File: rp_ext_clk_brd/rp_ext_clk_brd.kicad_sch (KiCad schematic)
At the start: 3 parts, among them J1 8526-4500PL, U1 SN65LVDS122D, Y1 AK7DAF1-125.0000

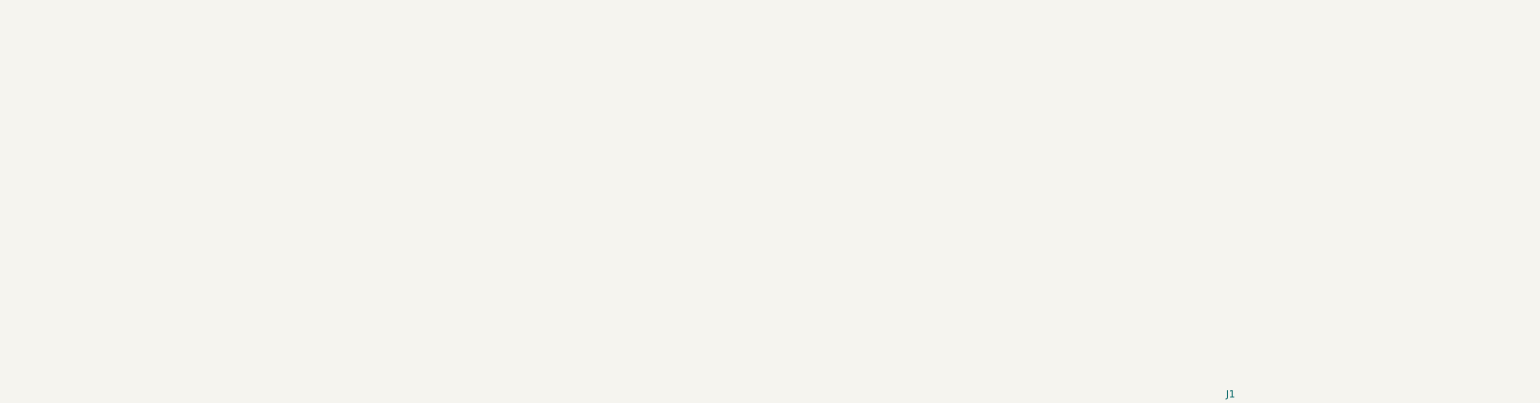
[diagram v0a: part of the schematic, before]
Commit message: adding decoupling and power supply
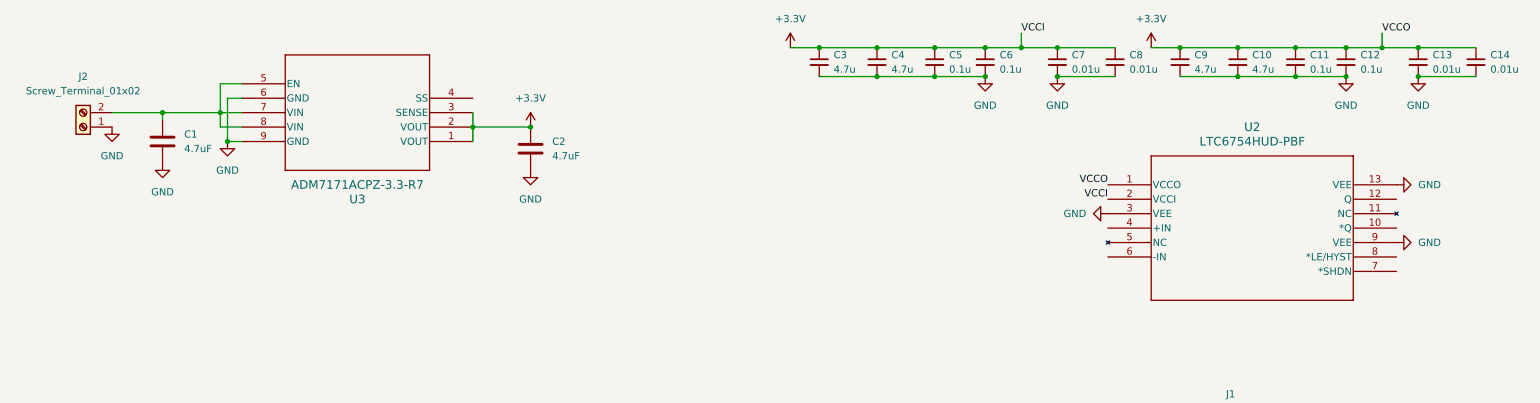
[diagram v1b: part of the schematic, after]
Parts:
- added C1, C2: 4.7uF, Capacitor_SMD:C_0805_2012Metric, symbol Device:C
- added C10, C3, C4, C9: 4.7u, Capacitor_SMD:C_1210_3225Metric, symbol Device:C_Small
- added C11, C12, C5, C6: 0.1u, Capacitor_SMD:C_1210_3225Metric, symbol Device:C_Small
- added C13, C14, C7, C8: 0.01u, Capacitor_SMD:C_0603_1608Metric, symbol Device:C_Small
- added J2: Screw_Terminal_01x02, TerminalBlock:TerminalBlock_MaiXu_MX126-5.0-02P_1x02_P5.00mm, symbol Connector:Screw_Terminal_01x02
- added U2: LTC6754HUD-PBF, LTC6754:QFN12_UD_ADI, symbol LTC6754:LTC6754HUD-PBF
- added U3: ADM7171ACPZ-3.3-R7, ADM7171:CP-8-21_ADI, symbol ADM7171ACPZ:ADM7171ACPZ-3.3-R7
- U1: footprint D16 -> SN65LVDS122:D16
- Y1: footprint AK7DAF1-125.0000:XTAL_AK7DAF1-125.0000 -> xtal_ak7daf1-125MHz:XTAL_AK7DAF1-125.0000
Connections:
- new net: C1.1, J2.2 (Pin_2), U3.5 (EN), U3.7 (VIN), U3.8 (VIN)
- new net +3.3V: C10.1, C11.1, C12.1, C13.1, C14.1, C2.1, C3.1, C4.1, C5.1, C6.1, C7.1, C8.1, C9.1, U2.1 (VCCO), U2.2 (VCCI), U3.1 (VOUT), U3.2 (VOUT), U3.3 (SENSE)
- new net GND: C1.2, C10.2, C11.2, C12.2, C13.2, C14.2, C2.2, C3.2, C4.2, C5.2, C6.2, C7.2, C8.2, C9.2, J2.1 (Pin_1), U2.13 (VEE), U2.3 (VEE), U2.9 (VEE), U3.6 (GND), U3.9 (GND)

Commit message: further changes
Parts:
- added C15, C16: 0.1u, Capacitor_SMD:C_1210_3225Metric, symbol Device:C_Small
- added C17: 0.01 uF, Capacitor_SMD:C_0603_1608Metric, symbol Device:C_Small
- added C18: 0.1 uF, Capacitor_SMD:C_1206_3216Metric, symbol Device:C_Small
- added C19: 1 uF, Capacitor_SMD:C_1206_3216Metric, symbol Device:C_Small
- added C20: 10 uF, CAP_TPS_D_AVX, symbol Device:C_Polarized
- added C21: 0.001 uF, Capacitor_SMD:C_0603_1608Metric, symbol Device:C_Small
- added C22: 68 uF, CAP_593_D:CAP_593D-D_VSS-M, symbol Device:C_Polarized
- added R1, R2, R3, R4: 20k, symbol Device:R_Small
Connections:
- net +3.3V: now also U1.15 (VCC), U1.16 (VCC), Y1.1 (OE), Y1.6 (VDD), C15.1, C16.1, C17.1, C18.1, C19.1, C20.1, C21.1, C22.1, R1.1, R3.1
- net GND: now also U1.8 (GND), U1.9 (GND), Y1.3 (GND), C15.2, C16.2, C17.2, C18.2, C19.2, C20.2, C21.2, C22.2, R2.2, R4.2
- net Q_N: now reaches U2.10 (*Q)
- net Q_N: now also U1.2 (1A)
- net Q_P: now reaches U2.12 (Q)
- net Q_P: now also U1.1 (1B)
- net at U2.4 (+IN): now also R1.2, R2.1
- net at U2.6 (-IN): now also R3.2, R4.1

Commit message: schematic almost done
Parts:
- removed U1: SN65LVDS122D, SN65LVDS122:D16, symbol SN65LVDS122:SN65LVDS122D
- added C23: 0.1 uF, symbol Device:C_Small
- added C24: 0.1 uF, Capacitor_SMD:C_1206_3216Metric, symbol Device:C_Small
- added J3: EXT_Connector_1, 8526-4500PL:3M_8526-4500PL, symbol 8526-4500PL:8526-4500PL
- added J4: Conn_Coaxial, symbol Connector:Conn_Coaxial
- added J5: PPS_In, symbol Connector:Conn_Coaxial
- added JP1, JP2, JP3: Jumper_3_Open, symbol Jumper:Jumper_3_Open
- added U1: SN65LVDT122D, D16, symbol SN65LVDT122:SN65LVDT122D
- added U4: SN74LVC1G07DBVR, DBV0005A_N, symbol SN74LVC1G07:SN74LVC1G07DBVR
- J1: value 8526-4500PL -> EXT_Connector_2
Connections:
- net +3.3V: now also JP1.3 (B), JP2.3 (B), JP3.3 (B), U1.15 (VCC), U1.16 (VCC)
- net GND: now also J1.1, J1.16, J1.2, J1.5, J1.6, C24.2, J3.1, J3.2, J4.2 (Ext), J5.2 (Ext), JP1.1 (A), JP2.1 (A), JP3.1 (A), U1.8 (GND), U1.9 (GND), U4.3 (GND)
- net Q_N: now also U1.2 (1A)
- net Q_P: now also U1.1 (1B)
- net at Y1.4 (OUT): now also U1.6 (2A)
- net at Y1.5 (COMP_OUT): now also U1.7 (2B)
- net at R1.2, R2.1, U2.4 (+IN): now also C23.2
- net AO1: now reaches J1.10
- net AIN2: now reaches J1.11
- net AIN3: now reaches J1.12
- net AIN0: now reaches J1.13
- net AIN1: now reaches J1.14
- net EXT_COM_MODE: now reaches J1.15
- net I2C_SDL_RP: now reaches J1.17
- net I2C_SDA_RP: now reaches J1.18
- net UART_TX: now reaches J1.19
- net UART_RX: now reaches J1.20
- net SPI_CLK: now reaches J1.21
- net SPI_CS: now reaches J1.22
- net SPI_MOSI: now reaches J1.23
- net SPI_MISO: now reaches J1.24
- net +5V: now reaches J1.25
- net -3.4V: now reaches J1.26
- net RP_EXT_CLK_P: now reaches J1.3
- net RP_EXT_CLK_P: now also U1.14 (1Y)
- net RP_EXT_CLK_N: now reaches J1.4
- net RP_EXT_CLK_N: now also U1.13 (1Z)
- net AO2: now reaches J1.7
- net AO3: now reaches J1.8
- net AO0: now reaches J1.9
- new net: JP3.2 (C), U1.4 (1DE)
- new net: JP2.2 (C), U1.3 (S0)
- new net: JP1.2 (C), U1.5 (S1)
- new net: J5.1 (In), U4.2 (A)
- new net: C23.1, J4.1 (In)
- new net +3.3V_RP: C24.1, J3.25, J3.26, U4.5 (VCC)
- new net DIO0_N: J3.23
- new net DIO0_P: J3.24
- new net DIO1_N: J3.21
- new net DIO1_P: J3.22, U4.4 (Y)
- new net DIO2_N: J3.19
- new net DIO2_P: J3.20
- new net DIO3_N: J3.17
- new net DIO3_P: J3.18
- new net DIO4_N: J3.15
- new net DIO4_P: J3.16
- new net DIO5_N: J3.13
- new net DIO5_P: J3.14
- new net DIO6_N: J3.11
- new net DIO6_P: J3.12
- new net DIO7_N: J3.9
- new net DIO7_P: J3.10
- no-connect marks 0 -> 8
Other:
- moved on the sheet: J1

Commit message: assigned bom for capacitors
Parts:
- added JP4: Jumper_3_Open, symbol Jumper:Jumper_3_Open
- added R5: 4.7k, symbol Device:R_Small
- C23: value 0.1 uF -> 0.01 uF; footprint (none) -> Capacitor_SMD:C_0603_1608Metric
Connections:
- net +3.3V: now also JP4.3 (B)
- net +3.3V_RP: now also R5.1
- net DIO1_P: no longer U4.4 (Y)
- net GND: now also JP4.1 (A)
- net at U1.12 (2DE): now also JP4.2 (C)
- net DIO1_N renamed 1PPS
- net 1PPS: now also U4.4 (Y), R5.2

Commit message: netlist compiled, exported to pcb
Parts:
- removed J4: Conn_Coaxial, symbol Connector:Conn_Coaxial
- removed J5: PPS_In, symbol Connector:Conn_Coaxial
- added J4, J5: 732512120, Conn_Coax_MLX:CONN-732513152_MOL, symbol Conn_Coax_Edge_MLX:732512120
- C20: footprint CAP_TPS_D_AVX -> CAP_TPS_D_AVX:CAP_TPS_D_AVX
- C22: footprint CAP_593_D:CAP_593D-D_VSS-M -> CAP_593_D_v1:CAP_593D-D_VSS
- J2: footprint TerminalBlock:TerminalBlock_MaiXu_MX126-5.0-02P_1x02_P5.00mm -> TerminalBlock_CUI:TerminalBlock_CUI_TB007-508-02_1x02_P5.08mm_Horizontal
- JP1, JP2, JP3, JP4: footprint (none) -> Connector_PinHeader_2.54mm:PinHeader_1x03_P2.54mm_Vertical
- R1, R2, R3, R4, R5: footprint (none) -> Resistor_SMD:R_0603_1608Metric
- U1: footprint D16 -> SN65LVDT122:D16
- U2: footprint LTC6754:QFN12_UD_ADI -> LT6594:QFN12_UD_ADI
- U4: footprint DBV0005A_N -> SN74LVC1G07DBVR:DBV0005A_L
- Y1: footprint xtal_ak7daf1-125MHz:XTAL_AK7DAF1-125.0000 -> AKDAF125:XTAL_AK7DAF1-125.0000
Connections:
- net GND: now also J4.2, J4.3, J5.2, J5.3
- net XTAL_P: now reaches U1.6 (2A), Y1.4 (OUT)
- net XTAL_N: now reaches U1.7 (2B), Y1.5 (COMP_OUT)
- net at U4.2 (A): now also J5.1
- net at C23.1: now also J4.1

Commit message: started routing
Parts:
- removed J2: Screw_Terminal_01x02, TerminalBlock_CUI:TerminalBlock_CUI_TB007-508-02_1x02_P5.08mm_Horizontal, symbol Connector:Screw_Terminal_01x02
- removed J4, J5: 732512120, Conn_Coax_MLX:CONN-732513152_MOL, symbol Conn_Coax_Edge_MLX:732512120
- added J2: 1860196, 1860196:1860196, symbol 1860196:1860196
- added J4, J5: Conn_Coaxial, Connector_Coaxial:SMA_Samtec_SMA-J-P-H-ST-EM1_EdgeMount, symbol Connector:Conn_Coaxial
- added R6: 49.9, Resistor_SMD:R_0603_1608Metric, symbol Device:R_Small
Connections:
- net GND: now also J2.2, J4.2 (Ext), J5.2 (Ext), R6.2
- net XTAL_N: now also U1.6 (2A); no longer U1.7 (2B)
- net XTAL_P: now also U1.7 (2B); no longer U1.6 (2A)
- net at U4.2 (A): now also J5.1 (In), R6.1
- net at C1.1, U3.5 (EN), U3.7 (VIN)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: now also J2.1
- net at C23.1: now also J4.1 (In)
